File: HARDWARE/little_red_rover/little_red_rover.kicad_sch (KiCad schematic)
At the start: 61 parts, among them J1 USB_C_Receptacle_USB2.0_14P, J2 Conn_01x04_Socket, J5 Conn_01x01_Socket, J6 Conn_01x01_Socket, J7 Conn_01x06, J8 Conn_02x12_Odd_Even, J9 Conn_01x06, Q1 PMOS, Q2 PMOS, SW1 SW_Push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

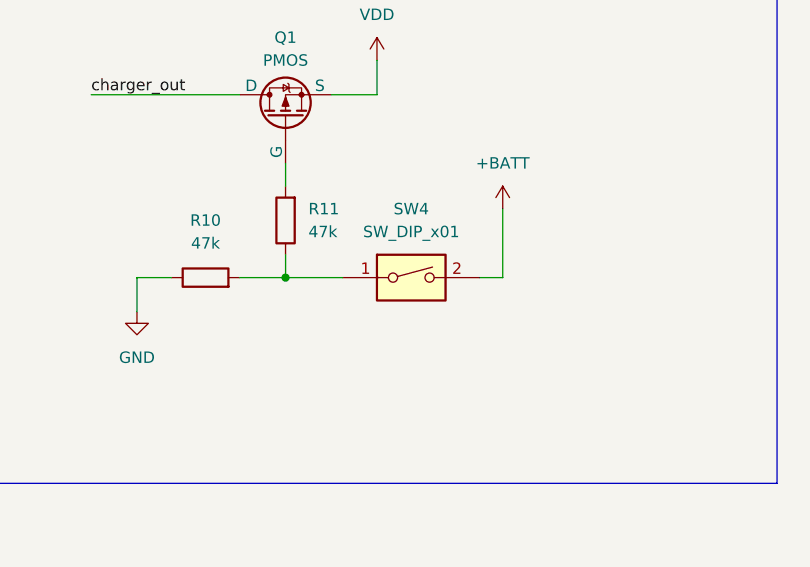
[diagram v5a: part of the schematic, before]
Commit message: Update layout: route schematic changes
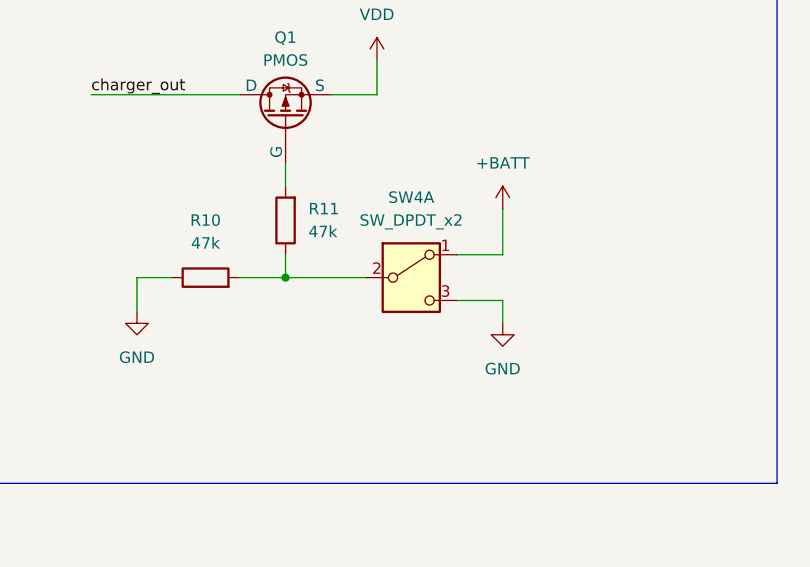
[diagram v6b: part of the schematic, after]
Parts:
- removed SW4: SW_DIP_x01, Button_Switch_SMD:SW_SPDT_PCM12, symbol Switch:SW_DIP_x01
- added SW4: SW_DPDT_x2, Button_Switch_SMD:SW_SPDT_PCM12, symbol Switch:SW_DPDT_x2
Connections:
- net +BATT: now also SW4.1 (A)
- net GND: now also SW4.3 (C)
- net at R10.2, R11.1: now also SW4.2 (B)
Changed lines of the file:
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@@
     (stroke (width 0) (type default))
   )
+  (wire (pts (xy 510.54 170.18) (xy 510.54 167.64))
+    (stroke (width 0) (type default))
+  )
   (wire (pts (xy 355.6 105.41) (xy 355.6 107.95))
     (stroke (width 0) (type default))
@@
     (stroke (width 0) (type default))
   )
-  (wire (pts (xy 486.41 165.1) (xy 492.76 165.1))
+  (wire (pts (xy 486.41 165.1) (xy 495.3 165.1))
     (stroke (width 0) (type default))
   )
@@
     (stroke (width 0) (type default))
   )
-  (wire (pts (xy 508 165.1) (xy 510.54 165.1))
+  (wire (pts (xy 505.46 162.56) (xy 510.54 162.56))
     (stroke (width 0) (type default))
   )
@@
     (stroke (width 0) (type default))
   )
+  (wire (pts (xy 510.54 167.64) (xy 505.46 167.64))
+    (stroke (width 0) (type default))
+  )
   (wire (pts (xy 269.24 76.2) (xy 269.24 77.47))
     (stroke (width 0) (type default))
@@
     (stroke (width 0) (type default))
   )
-  (wire (pts (xy 510.54 165.1) (xy 510.54 157.48))
+  (wire (pts (xy 510.54 162.56) (xy 510.54 157.48))
     (stroke (width 0) (type default))
   )
@@
     )
   )
+  (symbol (lib_id "power:GND") (at 510.54 170.18 0) (unit 1)
+    (in_bom yes) (on_board yes) (dnp no) (fields_autoplaced)
+    (property "Reference" "#PWR051" (at 510.54 176.53 0)
+      (effects (font (size 1.27 1.27)) hide)
+    )
+    (property "Value" "GND" (at 510.54 175.26 0)
+      (effects (font (size 1.27 1.27)))
+    )
+    (property "Footprint" "" (at 510.54 170.18 0)
+      (effects (font (size 1.27 1.27)) hide)
+    )
+    (property "Datasheet" "" (at 510.54 170.18 0)
+      (effects (font (size 1.27 1.27)) hide)
+    )
+    (pin "1")
+    (instances
+      (project "little_red_rover"
+        (path "/6f482c50-19c8-43f6-b4b5-8739f6fb7866"
+          (reference "#PWR051") (unit 1)
+        )
+      )
+    )
+  )
   (symbol (lib_id "power:GND") (at 251.46 110.49 0) (unit 1)
     (in_bom yes) (on_board yes) (dnp no)
@@
     )
   )
+  (symbol (lib_id "Switch:SW_DPDT_x2") (at 500.38 165.1 0) (unit 1)
+    (in_bom yes) (on_board yes) (dnp no) (fields_autoplaced)
+    (property "Reference" "SW4" (at 500.38 156.21 0)
+      (effects (font (size 1.27 1.27)))
+    )
+    (property "Value" "SW_DPDT_x2" (at 500.38 158.75 0)
+      (effects (font (size 1.27 1.27)))
+    )
+    (property "Footprint" "Button_Switch_SMD:SW_SPDT_PCM12" (at 500.38 165.1 0)
+      (effects (font (size 1.27 1.27)) hide)
+    )
+    (property "Datasheet" "~" (at 500.38 165.1 0)
+      (effects (font (size 1.27 1.27)) hide)
+    )
+    (property "LCSC" "C431541" (at 500.38 165.1 0)
+      (effects (font (size 1.27 1.27)) hide)
+    )
+    (pin "4")
+    (pin "3")
+    (pin "5")
+    (pin "6")
+    (pin "1")
+    (pin "2")
+    (instances
+      (project "little_red_rover"
+        (path "/6f482c50-19c8-43f6-b4b5-8739f6fb7866"
+          (reference "SW4") (unit 1)
+        )
+      )
+    )
+  )
   (symbol (lib_id "Mechanical:MountingHole") (at 481.33 309.88 0) (unit 1)
     (in_bom yes) (on_board yes) (dnp no) (fields_autoplaced)
@@
         )
       )
-    )
-  )
-  (symbol (lib_id "Switch:SW_DIP_x01") (at 500.38 165.1 0) (unit 1)
-    (in_bom yes) (on_board yes) (dnp no) (fields_autoplaced)
-    (property "Reference" "SW4" (at 500.38 157.48 0)
-      (effects (font (size 1.27 1.27)))
-    )
-    (property "Value" "SW_DIP_x01" (at 500.38 160.02 0)
-      (effects (font (size 1.27 1.27)))
-    )
-    (property "Footprint" "Button_Switch_SMD:SW_SPDT_PCM12" (at 500.38 165.1 0)
-      (effects (font (size 1.27 1.27)) hide)
-    )
-    (property "Datasheet" "~" (at 500.38 165.1 0)
-      (effects (font (size 1.27 1.27)) hide)
-    )
-    (property "LCSC" "C431541" (at 500.38 165.1 0)
-      (effects (font (size 1.27 1.27)) hide)
-    )
-    (pin "1")
-    (pin "2")
-    (instances
-      (project "little_red_rover"
-        (path "/6f482c50-19c8-43f6-b4b5-8739f6fb7866"
-          (reference "SW4") (unit 1)
-        )
-      )

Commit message: Update layout: Correct transistor pin numbers, replace hand solder esp footprint.
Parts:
- removed Q1, Q2: PMOS, Package_TO_SOT_SMD:SOT-23_Handsoldering, symbol Simulation_SPICE:PMOS
- added Q1, Q2: PMOS, Package_TO_SOT_SMD:TSOT-23_HandSoldering, symbol digikey_imports:PMOS
- U10: footprint Espressif:ESP32-S2-MINI-1_HandSoldering -> Espressif:ESP32-S3-MINI-1
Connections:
- net +BATT: now also Q2.2 (S)
- net VDD: now also Q1.2 (S)
- net bat_+: now also Q2.3 (D)
- net charger_out: now also Q1.3 (D)
- net at R6.2: now also Q2.1 (G)
- net at R11.2: now also Q1.1 (G)
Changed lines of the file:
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@@
-    )
-  )
-  (symbol (lib_id "Simulation_SPICE:PMOS") (at 419.1 154.94 90) (unit 1)
-    (in_bom yes) (on_board yes) (dnp no) (fields_autoplaced)
-    (property "Reference" "Q2" (at 419.1 146.05 90)
-      (effects (font (size 1.27 1.27)))
-    )
-    (property "Value" "PMOS" (at 419.1 148.59 90)
-      (effects (font (size 1.27 1.27)))
-    )
-    (property "Footprint" "Package_TO_SOT_SMD:SOT-23_Handsoldering" (at 416.56 149.86 0)
-      (effects (font (size 1.27 1.27)) hide)
-    )
-    (property "Datasheet" "https://ngspice.sourceforge.io/docs/ngspice-html-manual/manual.xhtml#cha_MOSFETs" (at 431.8 154.94 0)
-      (effects (font (size 1.27 1.27)) hide)
-    )
-    (property "Sim.Device" "PMOS" (at 436.245 154.94 0)
-      (effects (font (size 1.27 1.27)) hide)
-    )
-    (property "Sim.Type" "VDMOS" (at 438.15 154.94 0)
-      (effects (font (size 1.27 1.27)) hide)
-    )
-    (property "Sim.Pins" "1=D 2=G 3=S" (at 434.34 154.94 0)
-      (effects (font (size 1.27 1.27)) hide)
-    )
-    (property "JLC" "SOT-23" (at 419.1 154.94 0)
-      (effects (font (size 1.27 1.27)) hide)
-    )
-    (property "LCSC" "C347476" (at 419.1 154.94 0)
-      (effects (font (size 1.27 1.27)) hide)
-    )
-    (pin "1")
-    (pin "2")
-    (pin "3")
-    (instances
-      (project "little_red_rover"
-        (path "/6f482c50-19c8-43f6-b4b5-8739f6fb7866"
-          (reference "Q2") (unit 1)
-        )
-      )
     )
   )
@@
         (path "/6f482c50-19c8-43f6-b4b5-8739f6fb7866"
           (reference "#PWR025") (unit 1)
-        )
-      )
-    )
-  )
-  (symbol (lib_id "Simulation_SPICE:PMOS") (at 486.41 147.32 90) (unit 1)
-    (in_bom yes) (on_board yes) (dnp no) (fields_autoplaced)
-    (property "Reference" "Q1" (at 486.41 138.43 90)
-      (effects (font (size 1.27 1.27)))
-    )
-    (property "Value" "PMOS" (at 486.41 140.97 90)
-      (effects (font (size 1.27 1.27)))
-    )
-    (property "Footprint" "Package_TO_SOT_SMD:SOT-23_Handsoldering" (at 483.87 142.24 0)
-      (effects (font (size 1.27 1.27)) hide)
-    )
-    (property "Datasheet" "https://ngspice.sourceforge.io/docs/ngspice-html-manual/manual.xhtml#cha_MOSFETs" (at 499.11 147.32 0)
-      (effects (font (size 1.27 1.27)) hide)
-    )
-    (property "Sim.Device" "PMOS" (at 503.555 147.32 0)
-      (effects (font (size 1.27 1.27)) hide)
-    )
-    (property "Sim.Type" "VDMOS" (at 505.46 147.32 0)
-      (effects (font (size 1.27 1.27)) hide)
-    )
-    (property "Sim.Pins" "1=D 2=G 3=S" (at 501.65 147.32 0)
-      (effects (font (size 1.27 1.27)) hide)
-    )
-    (property "JLC" "SOT-23" (at 486.41 147.32 0)
-      (effects (font (size 1.27 1.27)) hide)
-    )
-    (property "LCSC" "C347476" (at 486.41 147.32 0)
-      (effects (font (size 1.27 1.27)) hide)
-    )
-    (pin "1")
-    (pin "2")
-    (pin "3")
-    (instances
-      (project "little_red_rover"
-        (path "/6f482c50-19c8-43f6-b4b5-8739f6fb7866"
-          (reference "Q1") (unit 1)
         )
       )
@@
     )
   )
+  (symbol (lib_id "digikey_imports:PMOS") (at 419.1 154.94 90) (unit 1)
+    (in_bom yes) (on_board yes) (dnp no) (fields_autoplaced)
+    (property "Reference" "Q2" (at 419.1 146.05 90)
+      (effects (font (size 1.27 1.27)))
+    )
+    (property "Value" "PMOS" (at 419.1 148.59 90)
+      (effects (font (size 1.27 1.27)))
+    )
+    (property "Footprint" "Package_TO_SOT_SMD:TSOT-23_HandSoldering" (at 416.56 149.86 0)
+      (effects (font (size 1.27 1.27)) hide)
+    )
+    (property "Datasheet" "https://ngspice.sourceforge.io/docs/ngspice-html-manual/manual.xhtml#cha_MOSFETs" (at 431.8 154.94 0)
+      (effects (font (size 1.27 1.27)) hide)
+    )
+    (property "Sim.Device" "PMOS" (at 436.245 154.94 0)
+      (effects (font (size 1.27 1.27)) hide)
+    )
+    (property "Sim.Type" "VDMOS" (at 438.15 154.94 0)
+      (effects (font (size 1.27 1.27)) hide)
+    )
+    (property "Sim.Pins" "1=D 2=G 3=S" (at 434.34 154.94 0)
+      (effects (font (size 1.27 1.27)) hide)
+    )
+    (pin "2")
+    (pin "1")
+    (pin "3")
+    (instances
+      (project "little_red_rover"
+        (path "/6f482c50-19c8-43f6-b4b5-8739f6fb7866"
+          (reference "Q2") (unit 1)
+        )
+      )
+    )
+  )
   (symbol (lib_id "LED:WS2812B-2020") (at 600.71 271.78 0) (unit 1)
     (in_bom yes) (on_board yes) (dnp no)
@@
     )
   )
+  (symbol (lib_id "digikey_imports:PMOS") (at 486.41 147.32 90) (unit 1)
+    (in_bom yes) (on_board yes) (dnp no) (fields_autoplaced)
+    (property "Reference" "Q1" (at 486.41 138.43 90)
+      (effects (font (size 1.27 1.27)))
+    )
+    (property "Value" "PMOS" (at 486.41 140.97 90)
+      (effects (font (size 1.27 1.27)))
+    )
+    (property "Footprint" "Package_TO_SOT_SMD:TSOT-23_HandSoldering" (at 483.87 142.24 0)
+      (effects (font (size 1.27 1.27)) hide)
+    )
+    (property "Datasheet" "https://ngspice.sourceforge.io/docs/ngspice-html-manual/manual.xhtml#cha_MOSFETs" (at 499.11 147.32 0)
+      (effects (font (size 1.27 1.27)) hide)
+    )
+    (property "Sim.Device" "PMOS" (at 503.555 147.32 0)
+      (effects (font (size 1.27 1.27)) hide)
+    )
+    (property "Sim.Type" "VDMOS" (at 505.46 147.32 0)
+      (effects (font (size 1.27 1.27)) hide)
+    )
+    (property "Sim.Pins" "1=D 2=G 3=S" (at 501.65 147.32 0)
+      (effects (font (size 1.27 1.27)) hide)
+    )
+    (pin "2")
+    (pin "1")
+    (pin "3")
+    (instances
+      (project "little_red_rover"
+        (path "/6f482c50-19c8-43f6-b4b5-8739f6fb7866"
+          (reference "Q1") (unit 1)
+        )
+      )
+    )
+  )
   (symbol (lib_id "Device:C") (at 130.81 332.74 0) (unit 1)
     (in_bom yes) (on_board yes) (dnp no) (fields_autoplaced)
@@
       (effects (font (size 1.27 1.27)) (justify left))
     )
-    (property "Footprint" "Espressif:ESP32-S2-MINI-1_HandSoldering" (at 113.03 165.1 0)
-      (effects (font (size 1.27 1.27)) hide)
-    )
+    (property "Footprint" "Espressif:ESP32-S3-MINI-1" (at 113.03 165.1 0)
+      (effects (font (size 1.27 1.27)) hide)
+    )

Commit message: PCB ordered, v 0.2.0
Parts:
- Q1, Q2: JLC (none) -> SOT-23; LCSC (none) -> C306862
- SW1, SW2, SW3: JLC - -> (none)
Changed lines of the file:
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@@
       (effects (font (size 1.27 1.27)) hide)
     )
-    (property "JLC" "-" (at 704.85 87.63 0)
+    (property "JLC" "" (at 704.85 87.63 0)
       (effects (font (size 1.27 1.27)) hide)
     )
@@
     )
     (property "Sim.Pins" "1=D 2=G 3=S" (at 434.34 154.94 0)
+      (effects (font (size 1.27 1.27)) hide)
+    )
+    (property "JLC" "SOT-23" (at 419.1 154.94 0)
+      (effects (font (size 1.27 1.27)) hide)
+    )
+    (property "LCSC" "C306862" (at 419.1 154.94 0)
       (effects (font (size 1.27 1.27)) hide)
     )
@@
     )
     (property "Sim.Pins" "1=D 2=G 3=S" (at 501.65 147.32 0)
+      (effects (font (size 1.27 1.27)) hide)
+    )
+    (property "JLC" "SOT-23" (at 486.41 147.32 0)
+      (effects (font (size 1.27 1.27)) hide)
+    )
+    (property "LCSC" "C306862" (at 486.41 147.32 0)
       (effects (font (size 1.27 1.27)) hide)
     )
@@
       (effects (font (size 1.27 1.27)) hide)
     )
-    (property "JLC" "-" (at 628.65 144.78 0)
+    (property "JLC" "" (at 628.65 144.78 0)
       (effects (font (size 1.27 1.27)) hide)
     )
@@
       (effects (font (size 1.27 1.27)) hide)
     )
-    (property "JLC" "-" (at 704.85 68.58 0)
-      (effects (font (size 1.27 1.27)) hide)
-    )
+    (property "JLC" "" (at 704.85 68.58 0)
+      (effects (font (size 1.27 1.27)) hide)
+    )
